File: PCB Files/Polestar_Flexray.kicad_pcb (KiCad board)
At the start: 4 copper layers, 98 x 58 mm, 84 parts, among them J1 JAE DX07S024XJ1R1100, J2 Molex 2125280400, J3 JAE MX34032NF4, J4 JAE MX34032NF4, K1 G5V-2-H1 DC12, K2 G5V-2-H1 DC12, K3 G5V-2-H1 DC12, Q1 DMN3200U-7, Q2 DMN3200U-7, Q3 DMP4015SSS-13, U1 Vishay DG419LEDY-T1-GE4, U2 Vishay DG419LEDY-T1-GE4, U3 LM53600LQDSXRQ1, U4 XIAO_RP2350, U5 TJA1082, U6 TJA1082, U8 TCAN4550-Q1, Y1 40MHz NX2016SA

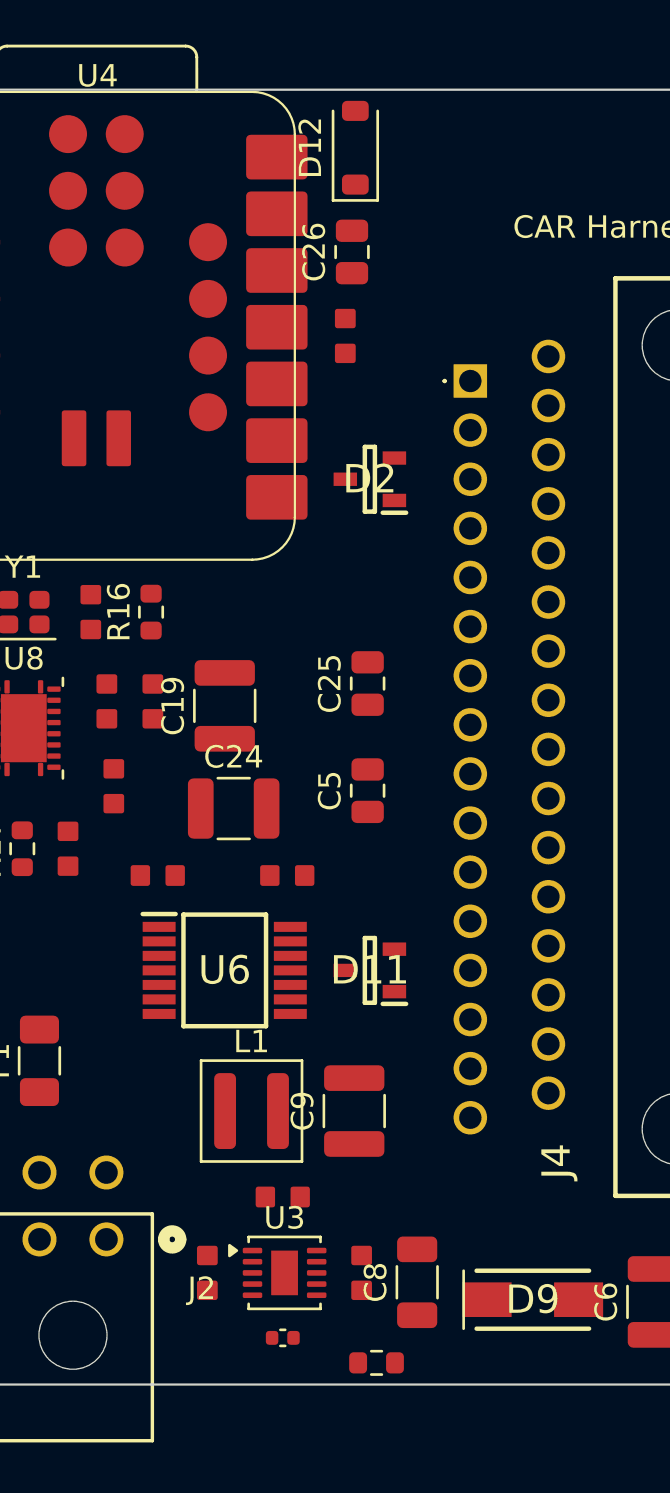
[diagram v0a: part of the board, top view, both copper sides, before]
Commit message: Add symbol and footprint libraries, project-local lib tables, U8 3D model
Libraries
- Added Library/Symbols (6 libraries, 17 custom symbols) and
  Library/Footprints.pretty (91 footprints; the 33 this design uses).
  Previously a clone could not resolve any custom symbol or footprint.
- Added project-local fp-lib-table and sym-lib-table in PCB Files/,
  resolving through ${KIPRJMOD}/../Library so the project opens on a
  fresh clone without editing global KiCad library tables.
- Verified: 33/33 custom footprints and 17/17 custom symbols resolve.

Board
- Assigned a 3D model to U8 (TCAN4550-Q1); it had none. The STEP is
  authored Y-up, so it carries rotate (xyz -90 0 0) to sit in KiCad's
  Z-up frame. Checked against the land pattern: the 3.5 x 4.5 mm body
  overhangs the 3.3 x 4.3 mm pads by 0.1 mm per side, as expected.
  The footprint itself is unchanged and still matches TI drawing
  4225320/A.
- Gave H1-H4 a proper library nickname. They were written with a bare
  lib_id of "MountingHole_3.2mm_M3", which no library could match.

3D model files are deliberately not included. 44 model references point
at a personal model directory (14 distinct files), so those parts render
as bare pads in the 3D viewer on a clone. Netlist, footprints and
fabrication outputs are unaffected.

Co-Authored-By: Claude Opus 5 <noreply@anthropic.com>
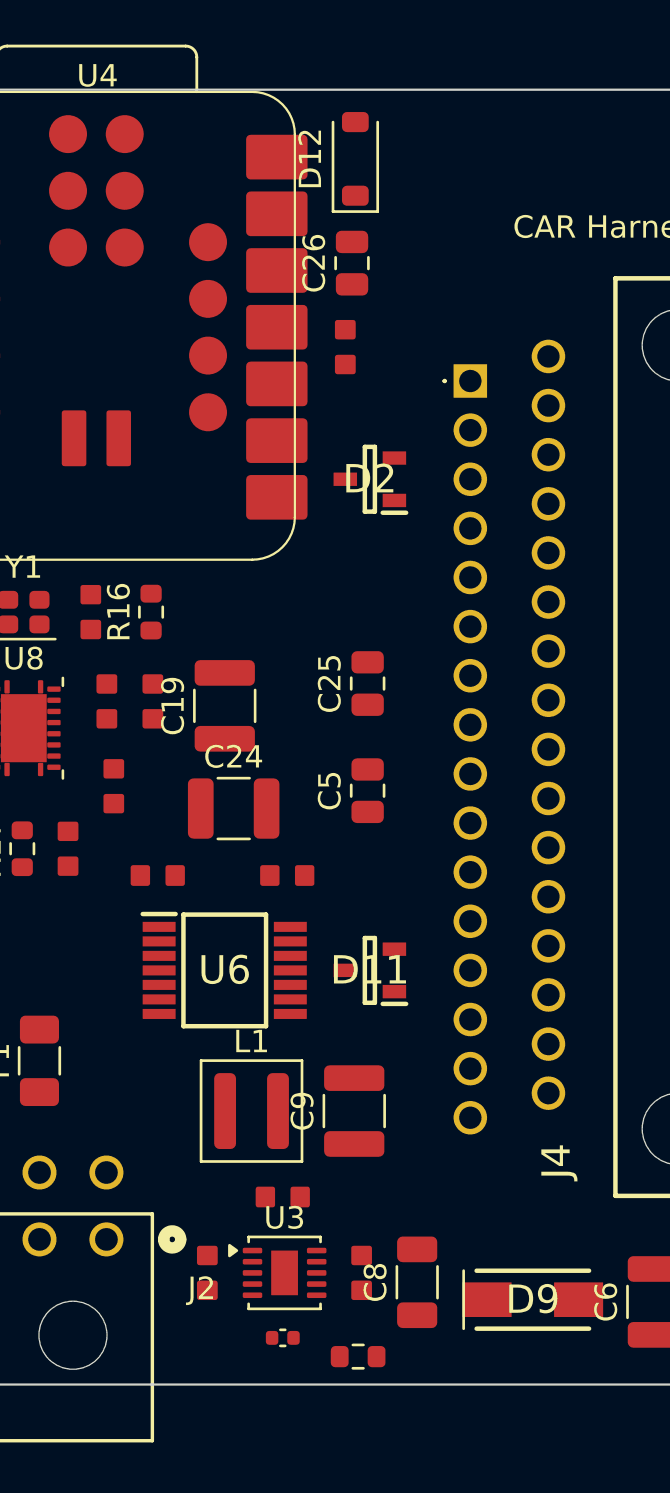
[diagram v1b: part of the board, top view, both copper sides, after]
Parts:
- H1, H2, H3, H4: footprint MountingHole_3.2mm_M3 -> MountingHole:MountingHole_3.2mm_M3
- moved R13 0.87 mm to (175.6, 126.2)
- moved C26 0.50 mm to (175.3, 77.3)
- moved C7 0.50 mm to (175.0, 81.0)
- moved D12 0.50 mm to (175.4, 72.6)
- turned C27 to 180 degrees
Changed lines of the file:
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@@
 		)
 	)
-	(footprint "MountingHole_3.2mm_M3"
+	(footprint "MountingHole:MountingHole_3.2mm_M3"
 		(layer "F.Cu")
 		(at 196.2 73.3)
@@
 	(footprint "Footprints:SAMS CL05B103KA5NNNC"
 		(layer "F.Cu")
-		(at 172.2 125.41)
+		(at 172.2 125.41 180)
 		(descr "Samsung 10nF capacitor")
 		(property "Reference" "C27"
@@
 		(duplicate_pad_numbers_are_jumpers no)
 		(fp_line
-			(start -0.107836 -0.36)
-			(end 0.107836 -0.36)
+			(start -0.107836 0.36)
+			(end 0.107836 0.36)
 			(stroke
 				(width 0.12)
@@
 		)
 		(fp_line
-			(start -0.107836 0.36)
-			(end 0.107836 0.36)
+			(start -0.107836 -0.36)
+			(end 0.107836 -0.36)
 			(stroke
 				(width 0.12)
@@
 		)
 		(fp_line
-			(start -0.91 -0.46)
-			(end 0.91 -0.46)
+			(start 0.91 0.46)
+			(end -0.91 0.46)
 			(stroke
 				(width 0.05)
@@
 		)
 		(fp_line
-			(start -0.91 0.46)
-			(end -0.91 -0.46)
+			(start 0.91 -0.46)
+			(end 0.91 0.46)
 			(stroke
 				(width 0.05)
@@
 		)
 		(fp_line
-			(start 0.91 -0.46)
-			(end 0.91 0.46)
+			(start -0.91 0.46)
+			(end -0.91 -0.46)
 			(stroke
 				(width 0.05)
@@
 		)
 		(fp_line
-			(start 0.91 0.46)
-			(end -0.91 0.46)
+			(start -0.91 -0.46)
+			(end 0.91 -0.46)
 			(stroke
 				(width 0.05)
@@
 		)
 		(fp_line
-			(start -0.5 -0.25)
-			(end 0.5 -0.25)
+			(start 0.5 0.25)
+			(end -0.5 0.25)
 			(stroke
 				(width 0.1)
@@
 		)
 		(fp_line
-			(start -0.5 0.25)
-			(end -0.5 -0.25)
+			(start 0.5 -0.25)
+			(end 0.5 0.25)
 			(stroke
 				(width 0.1)
@@
 		)
 		(fp_line
-			(start 0.5 -0.25)
-			(end 0.5 0.25)
+			(start -0.5 0.25)
+			(end -0.5 -0.25)
 			(stroke
 				(width 0.1)
@@
 		)
 		(fp_line
-			(start 0.5 0.25)
-			(end -0.5 0.25)
+			(start -0.5 -0.25)
+			(end 0.5 -0.25)
 			(stroke
 				(width 0.1)
@@
 		)
 		(pad "1" smd roundrect
-			(at -0.48 0)
+			(at -0.48 0 180)
 			(size 0.56 0.62)
 			(layers "F.Cu" "F.Mask" "F.Paste")
@@
 		)
 		(pad "2" smd roundrect
-			(at 0.48 0)
+			(at 0.48 0 180)
 			(size 0.56 0.62)
 			(layers "F.Cu" "F.Mask" "F.Paste")
@@
 	(footprint "Footprints:SCHOTTKY - 1A"
 		(layer "F.Cu")
-		(at 175.45 72.1 90)
+		(at 175.45 72.6 90)
 		(descr "Schottky rectifier, 40V, 1A")
 		(property "Reference" "D12"
@@
 	(footprint "Footprints:SAMS CL10B105KA8NNNC"
 		(layer "F.Cu")
-		(at 175 80.53 90)
+		(at 175 81.03 90)
 		(descr "Samsung 1uF capacitor")
 		(property "Reference" "C7"
@@
 		)
 	)
-	(footprint "MountingHole_3.2mm_M3"
+	(footprint "MountingHole:MountingHole_3.2mm_M3"
 		(layer "F.Cu")
 		(at 105.8 123.7)
@@
 	(footprint "Footprints:SAMS CL21B106KAYQNNE"
 		(layer "F.Cu")
-		(at 175.3 76.77 90)
+		(at 175.3 77.27 90)
 		(descr "Samsung 10uF 25V X7R capacitor (0805)")
 		(tags "capacitor")
@@
 		)
 	)
-	(footprint "MountingHole_3.2mm_M3"
+	(footprint "MountingHole:MountingHole_3.2mm_M3"
 		(layer "F.Cu")
 		(at 196.2 123.7)
@@
 	(footprint "Footprints:Rohm ESR03EZPJ104"
 		(layer "F.Cu")
-		(at 176.4 126.53)
+		(at 175.575 126.25)
 		(descr "Rohm 100K 150V 250mw resistor, ESR series")
 		(property "Reference" "R13"
@@
 		(sheetname "/")
 		(sheetfile "Polestar_Flexray.kicad_sch")
-		(units
-			(unit
-				(name "A")
-				(pins "4" "5" "6" "7" "8" "19" "2" "3" "9" "1" "20" "14" "16" "17" "18"
-					"11" "10" "12" "15" "21" "13"
-				)
-			)
-		)
 		(attr smd)
 		(duplicate_pad_numbers_are_jumpers no)
@@
 		)
 		(embedded_fonts no)
+		(model "${KICAD_USER_3D_MODELS}/TI TCAN4550RGYRQ1.step"
+			(offset
+				(xyz 0 0 0)
+			)
+			(scale
+				(xyz 1 1 1)
+			)
+			(rotate
+				(xyz -0 -0 -0)
+			)
+		)
 	)
 	(footprint "Footprints:SAMS CL21B106KAYQNNE"
@@
 		)
 	)
-	(footprint "MountingHole_3.2mm_M3"
+	(footprint "MountingHole:MountingHole_3.2mm_M3"
 		(layer "F.Cu")
 		(at 105.8 73.3)
@@
 		)
 	)
-	(gr_line
-		(start 105.8 69.5)
-		(end 196.2 69.5)
-		(stroke
-			(width 0.1)
-			(type default)
-		)
-		(layer "Edge.Cuts")
-	)
-	(gr_arc
-		(start 196.2 69.5)
-		(mid 198.887 70.613)
-		(end 200 73.3)
-		(stroke
-			(width 0.1)
-			(type default)
-		)
-		(layer "Edge.Cuts")
-	)
-	(gr_line
-		(start 200 73.3)
-		(end 200 123.7)
-		(stroke
-			(width 0.1)
-			(type default)
-		)
-		(layer "Edge.Cuts")
-	)
-	(gr_arc
-		(start 200 123.7)
-		(mid 198.887 126.387)
-		(end 196.2 127.5)
-		(stroke
-			(width 0.1)
-			(type default)
-		)
-		(layer "Edge.Cuts")
-	)
-	(gr_line
-		(start 196.2 127.5)
-		(end 105.8 127.5)
-		(stroke
-			(width 0.1)
-			(type default)
-		)
-		(layer "Edge.Cuts")
-	)
-	(gr_arc
-		(start 105.8 127.5)
-		(mid 103.113 126.387)
-		(end 102 123.7)
-		(stroke
-			(width 0.1)
-			(type default)
-		)
-		(layer "Edge.Cuts")
-	)
-	(gr_line
-		(start 102 123.7)
-		(end 102 73.3)
-		(stroke
-			(width 0.1)
-			(type default)
-		)
-		(layer "Edge.Cuts")
-	)
-	(gr_arc
-		(start 102 73.3)
-		(mid 103.113 70.613)
-		(end 105.8 69.5)
-		(stroke
-			(width 0.1)
-			(type default)
-		)
-		(layer "Edge.Cuts")
-	)
 	(footprint "Footprints:DMN3200U-7"
 		(layer "F.Cu")
@@
 		)
 	)
+	(gr_arc
+		(start 102 73.3)
+		(mid 103.113 70.613)
+		(end 105.8 69.5)
+		(stroke
+			(width 0.1)
+			(type default)
+		)
+		(layer "Edge.Cuts")
+	)
+	(gr_line
+		(start 102 123.7)
+		(end 102 73.3)
+		(stroke
+			(width 0.1)
+			(type default)
+		)
+		(layer "Edge.Cuts")
+	)
+	(gr_line
+		(start 105.8 69.5)
+		(end 196.2 69.5)
+		(stroke
+			(width 0.1)
+			(type default)
+		)
+		(layer "Edge.Cuts")
+	)
+	(gr_arc
+		(start 105.8 127.5)
+		(mid 103.113 126.387)
+		(end 102 123.7)
+		(stroke
+			(width 0.1)
+			(type default)
+		)
+		(layer "Edge.Cuts")
+	)
+	(gr_arc
+		(start 196.2 69.5)
+		(mid 198.887 70.613)
+		(end 200 73.3)
+		(stroke
+			(width 0.1)
+			(type default)
+		)
+		(layer "Edge.Cuts")
+	)
+	(gr_line
+		(start 196.2 127.5)
+		(end 105.8 127.5)
+		(stroke
+			(width 0.1)
+			(type default)
+		)
+		(layer "Edge.Cuts")
+	)
+	(gr_line
+		(start 200 73.3)
+		(end 200 123.7)
+		(stroke
+			(width 0.1)
+			(type default)
+		)
+		(layer "Edge.Cuts")
+	)
+	(gr_arc
+		(start 200 123.7)
+		(mid 198.887 126.387)
+		(end 196.2 127.5)
+		(stroke
+			(width 0.1)
+			(type default)
+		)
+		(layer "Edge.Cuts")
+	)
 	(gr_text "VIN"
 		(at 145 102 0)
@@
 		)
 		(polygon
-				(pts
-					(xy 105.8 69.45)
-					(xy 196.2 69.45)
-					(xy 196.702 69.4829)
-					(xy 197.196 69.5812)
-					(xy 197.673 69.7431)
-					(xy 198.125 69.9658)
-					(xy 198.544 70.2456)
-					(xy 198.922 70.5776)
-					(xy 199.254 70.9563)
-					(xy 199.534 71.375)
-					(xy 199.757 71.8267)
-					(xy 199.919 72.3035)
-					(xy 200.017 72.7975)
-					(xy 200.05 73.3)
-					(xy 200.05 123.7)
-					(xy 200.017 124.203)
-					(xy 199.919 124.697)
-					(xy 199.757 125.173)
-					(xy 199.534 125.625)
-					(xy 199.254 126.044)
-					(xy 198.922 126.422)
-					(xy 198.544 126.754)
-					(xy 198.125 127.034)
-					(xy 197.673 127.257)
-					(xy 197.196 127.419)
-					(xy 196.702 127.517)
-					(xy 196.2 127.55)
-					(xy 105.8 127.55)
-					(xy 105.297 127.517)
-					(xy 104.803 127.419)
-					(xy 104.327 127.257)
-					(xy 103.875 127.034)
-					(xy 103.456 126.754)
-					(xy 103.078 126.422)
-					(xy 102.746 126.044)
-					(xy 102.466 125.625)
-					(xy 102.243 125.173)
-					(xy 102.081 124.697)
-					(xy 101.983 124.203)
-					(xy 101.95 123.7)
-					(xy 101.95 73.3)
-					(xy 101.983 72.7975)
-					(xy 102.081 72.3035)
-					(xy 102.243 71.8267)
-					(xy 102.466 71.375)
-					(xy 102.746 70.9563)
-					(xy 103.078 70.5776)
-					(xy 103.456 70.2456)
-					(xy 103.875 69.9658)
-					(xy 104.327 69.7431)
-					(xy 104.803 69.5812)
-					(xy 105.297 69.4829)
-					(xy 105.8 69.45)
-				)
+			(pts
+				(xy 105.8 69.45) (xy 196.2 69.45) (xy 196.702 69.4829) (xy 197.196 69.5812) (xy 197.673 69.7431)
+				(xy 198.125 69.9658) (xy 198.544 70.2456) (xy 198.922 70.5776) (xy 199.254 70.9563) (xy 199.534 71.375)
+				(xy 199.757 71.8267) (xy 199.919 72.3035) (xy 200.017 72.7975) (xy 200.05 73.3) (xy 200.05 123.7)
+				(xy 200.017 124.203) (xy 199.919 124.697) (xy 199.757 125.173) (xy 199.534 125.625) (xy 199.254 126.044)
+				(xy 198.922 126.422) (xy 198.544 126.754) (xy 198.125 127.034) (xy 197.673 127.257) (xy 197.196 127.419)
+				(xy 196.702 127.517) (xy 196.2 127.55) (xy 105.8 127.55) (xy 105.297 127.517) (xy 104.803 127.419)
+				(xy 104.327 127.257) (xy 103.875 127.034) (xy 103.456 126.754) (xy 103.078 126.422) (xy 102.746 126.044)
+				(xy 102.466 125.625) (xy 102.243 125.173) (xy 102.081 124.697) (xy 101.983 124.203) (xy 101.95 123.7)
+				(xy 101.95 73.3) (xy 101.983 72.7975) (xy 102.081 72.3035) (xy 102.243 71.8267) (xy 102.466 71.375)
+				(xy 102.746 70.9563) (xy 103.078 70.5776) (xy 103.456 70.2456) (xy 103.875 69.9658) (xy 104.327 69.7431)
+				(xy 104.803 69.5812) (xy 105.297 69.4829)
 			)
+		)
 	)
 	(embedded_fonts no)
